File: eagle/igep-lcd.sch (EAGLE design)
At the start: 9 parts, among them IC1 LM1117IMPX-3.3, U1 SN74LVC8T245PW, U2 SN74LVC8T245PW, U3 SN74LVC8T245PW, U4 SN74LVC8T245PW

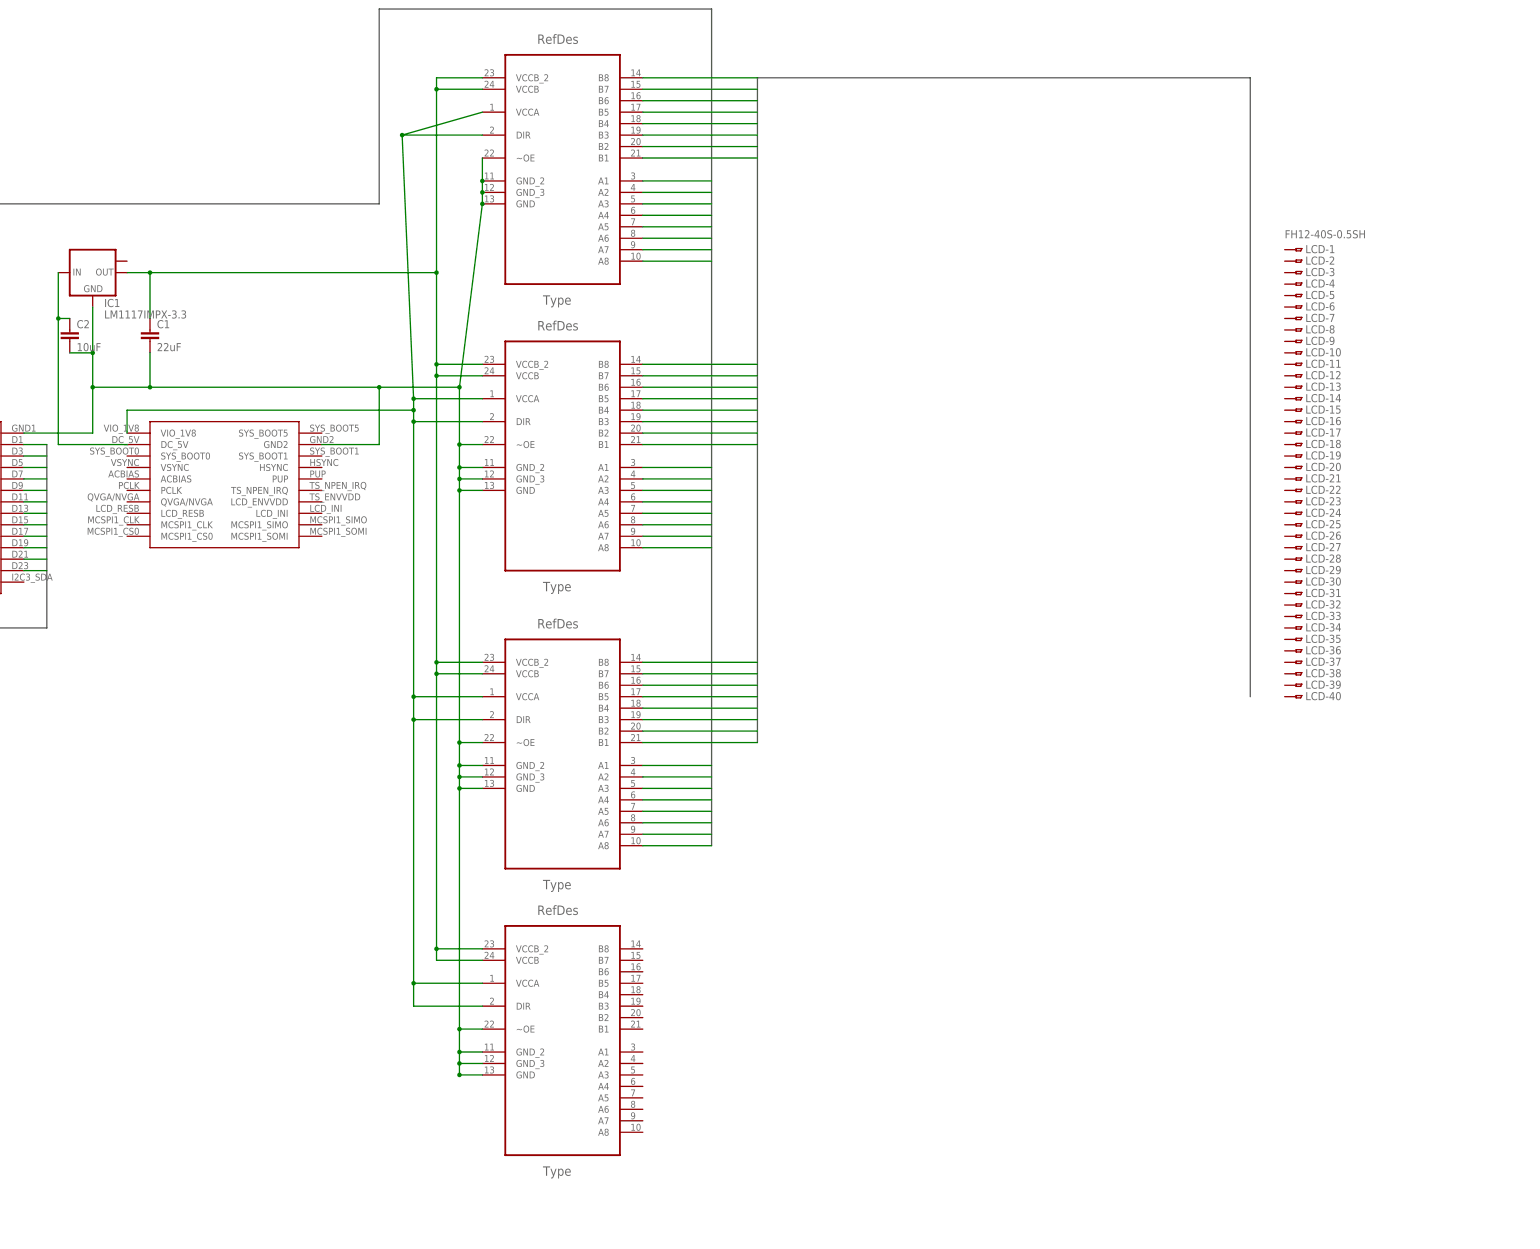
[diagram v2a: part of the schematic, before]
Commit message: Added all LCD data lines and clocks
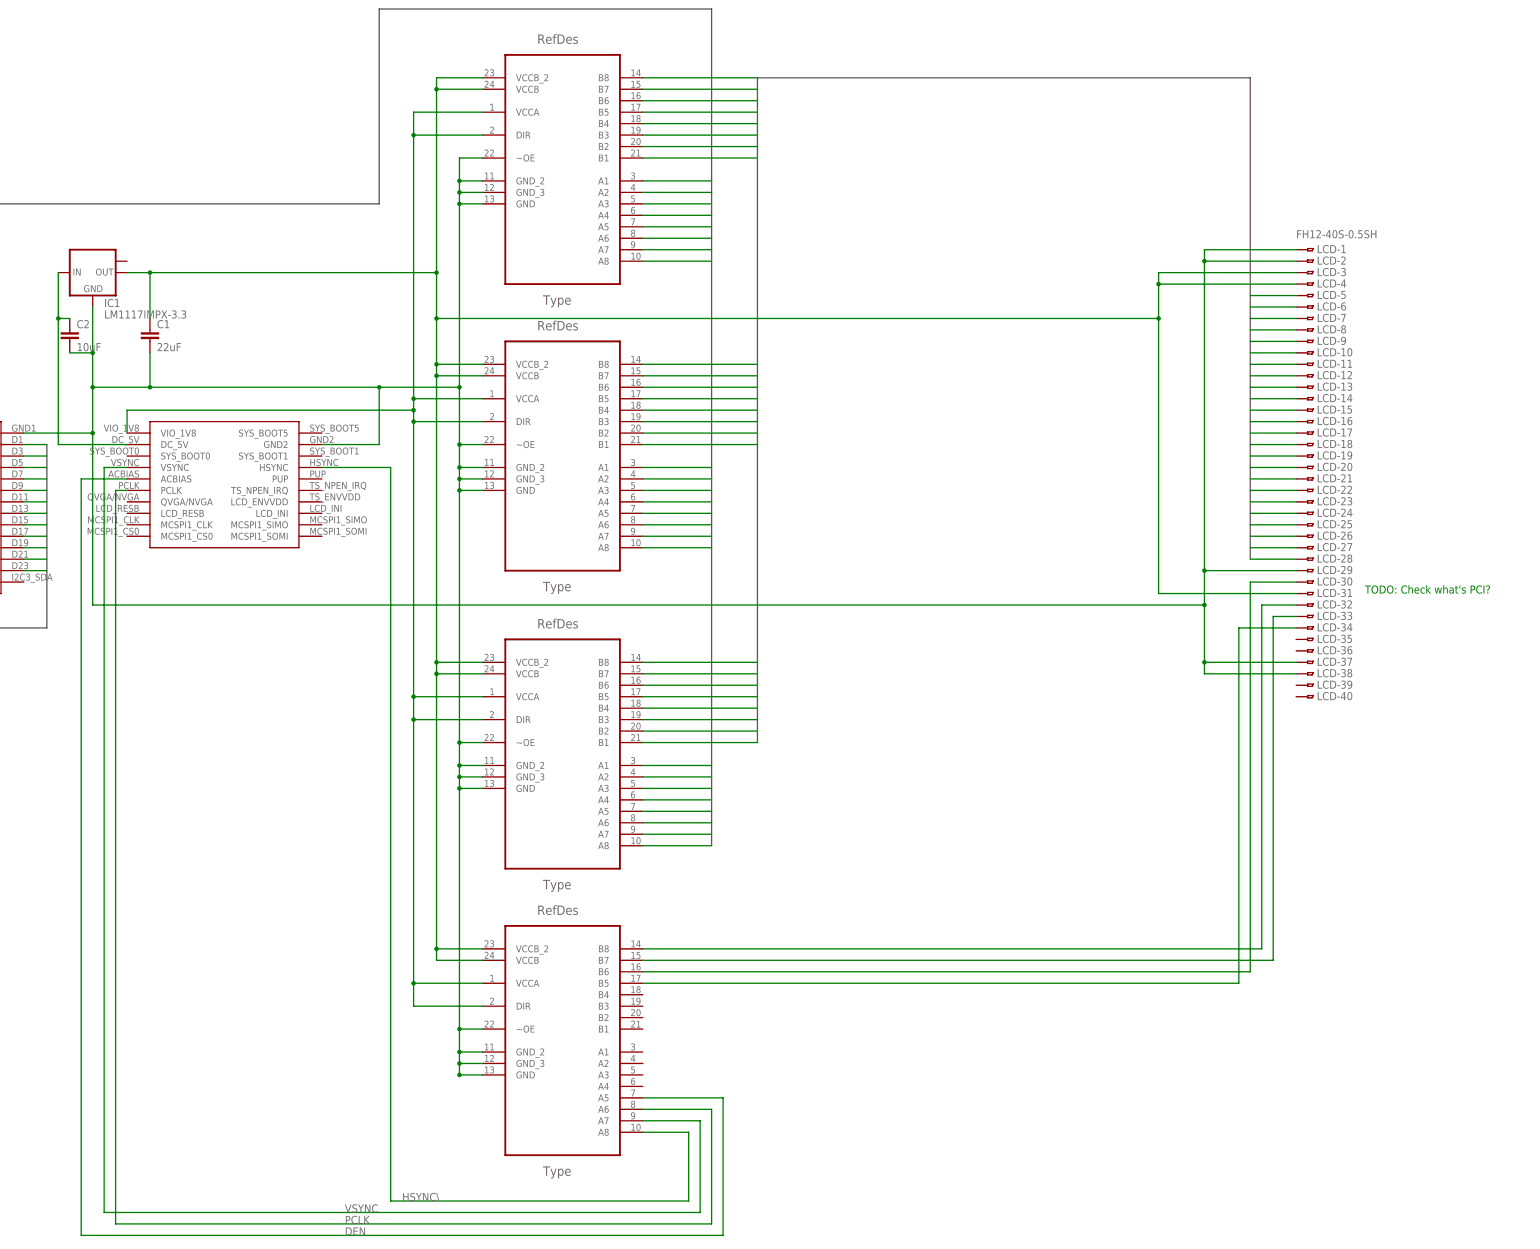
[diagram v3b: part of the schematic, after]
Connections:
- removed net N$6: C1.1, IC1.OUT, U1.VCCB, U1.VCCB_2, U2.VCCB, U2.VCCB_2, U3.VCCB, U3.VCCB_2, U4.VCCB, U4.VCCB_2
- new net DEN: U$1.ACBIAS, U4.A5
- new net HSYNC\: U$1.HSYNC, U4.A8
- new net IGEP_LCD_DATA0: U$1.D0, U1.A1
- new net IGEP_LCD_DATA1: U$1.D1, U1.A2
- new net IGEP_LCD_DATA10: U$1.D10, U2.A3
- new net IGEP_LCD_DATA11: U$1.D11, U2.A4
- new net IGEP_LCD_DATA12: U$1.D12, U2.A5
- new net IGEP_LCD_DATA13: U$1.D13, U2.A6
- new net IGEP_LCD_DATA14: U$1.D14, U2.A7
- new net IGEP_LCD_DATA15: U$1.D15, U2.A8
- new net IGEP_LCD_DATA16: U$1.D16, U3.A1
- new net IGEP_LCD_DATA17: U$1.D17, U3.A2
- new net IGEP_LCD_DATA18: U$1.D18, U3.A3
- new net IGEP_LCD_DATA19: U$1.D19, U3.A4
- new net IGEP_LCD_DATA2: U$1.D2, U1.A3
- new net IGEP_LCD_DATA20: U$1.D20, U3.A5
- new net IGEP_LCD_DATA21: U$1.D21, U3.A6
- new net IGEP_LCD_DATA22: U$1.D22, U3.A7
- new net IGEP_LCD_DATA23: U$1.D23, U3.A8
- new net IGEP_LCD_DATA3: U$1.D3, U1.A4
- new net IGEP_LCD_DATA4: U$1.D4, U1.A5
- new net IGEP_LCD_DATA5: U$1.D5, U1.A6
- new net IGEP_LCD_DATA6: U$1.D6, U1.A7
- new net IGEP_LCD_DATA7: U$1.D7, U1.A8
- new net IGEP_LCD_DATA8: U$1.D8, U2.A1
- new net IGEP_LCD_DATA9: U$1.D9, U2.A2
- new net N$10: LCD-30.1, U4.B6
- new net N$11: LCD-34.1, U4.B5
- new net N$3: C1.1, IC1.OUT, LCD-3.1, LCD-31.1, LCD-4.1, U1.VCCB, U1.VCCB_2, U2.VCCB, U2.VCCB_2, U3.VCCB, U3.VCCB_2, U4.VCCB, U4.VCCB_2
- new net N$5: LCD-32.1, U4.B8
- new net N$9: LCD-33.1, U4.B7
- new net PCLK: U$1.PCLK, U4.A6
- new net VSYNC: U$1.VSYNC, U4.A7
- net LCD_DATA0: now also LCD-21.1; no longer U$1.D0, U1.A1
- net LCD_DATA1: now also LCD-22.1; no longer U$1.D1, U1.A2
- net LCD_DATA10: now also LCD-15.1; no longer U$1.D10, U2.A3
- net LCD_DATA11: now also LCD-16.1; no longer U$1.D11, U2.A4
- net LCD_DATA12: now also LCD-17.1; no longer U$1.D12, U2.A5
- net LCD_DATA13: now also LCD-18.1; no longer U$1.D13, U2.A6
- net LCD_DATA14: now also LCD-19.1; no longer U$1.D14, U2.A7
- net LCD_DATA15: now also LCD-20.1; no longer U$1.D15, U2.A8
- net LCD_DATA16: now also LCD-5.1; no longer U$1.D16, U3.A1
- net LCD_DATA17: now also LCD-6.1; no longer U$1.D17, U3.A2
- net LCD_DATA18: now also LCD-7.1; no longer U$1.D18, U3.A3
- net LCD_DATA19: now also LCD-8.1; no longer U$1.D19, U3.A4
- net LCD_DATA2: now also LCD-23.1; no longer U$1.D2, U1.A3
- net LCD_DATA20: now also LCD-9.1; no longer U$1.D20, U3.A5
- net LCD_DATA21: now also LCD-10.1; no longer U$1.D21, U3.A6
- net LCD_DATA22: now also LCD-11.1; no longer U$1.D22, U3.A7
- net LCD_DATA23: now also LCD-12.1; no longer U$1.D23, U3.A8
- net LCD_DATA3: now also LCD-24.1; no longer U$1.D3, U1.A4
- net LCD_DATA4: now also LCD-25.1; no longer U$1.D4, U1.A5
- net LCD_DATA5: now also LCD-26.1; no longer U$1.D5, U1.A6
- net LCD_DATA6: now also LCD-27.1; no longer U$1.D6, U1.A7
- net LCD_DATA7: now also LCD-28.1; no longer U$1.D7, U1.A8
- net LCD_DATA8: now also LCD-13.1; no longer U$1.D8, U2.A1
- net LCD_DATA9: now also LCD-14.1; no longer U$1.D9, U2.A2
- net N$2: now also LCD-1.1, LCD-2.1, LCD-29.1, LCD-37.1, LCD-38.1
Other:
- note added: "TODO: Check what's PCI?"
- moved on the sheet: LCD-1, LCD-10, LCD-11, LCD-12, LCD-13, LCD-14, LCD-15, LCD-16, LCD-17, LCD-18, LCD-19, LCD-2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
